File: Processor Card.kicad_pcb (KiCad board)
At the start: 2 copper layers, 100 x 100 mm, 31 parts, among them J1 Conn_02x20_Odd_Even, U1 CDP1802/1806, U10 74LS573, U11 74LS138, U2 28C256, U3 62256, U4 62256, U5 74LS32, U6 74LS20, U7 74LS74, U8 74LS04, U9 74LS74

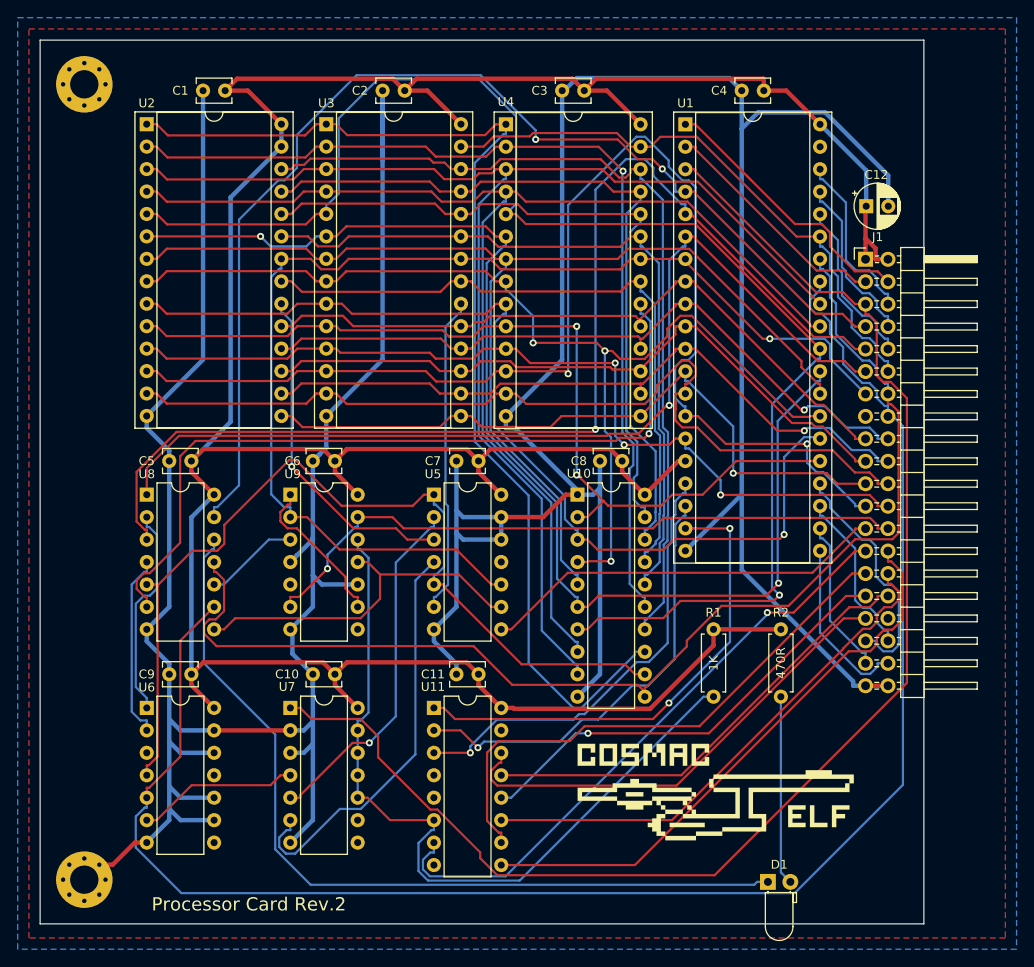
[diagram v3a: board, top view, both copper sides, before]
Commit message: Fix PCB / Schematic mismatch
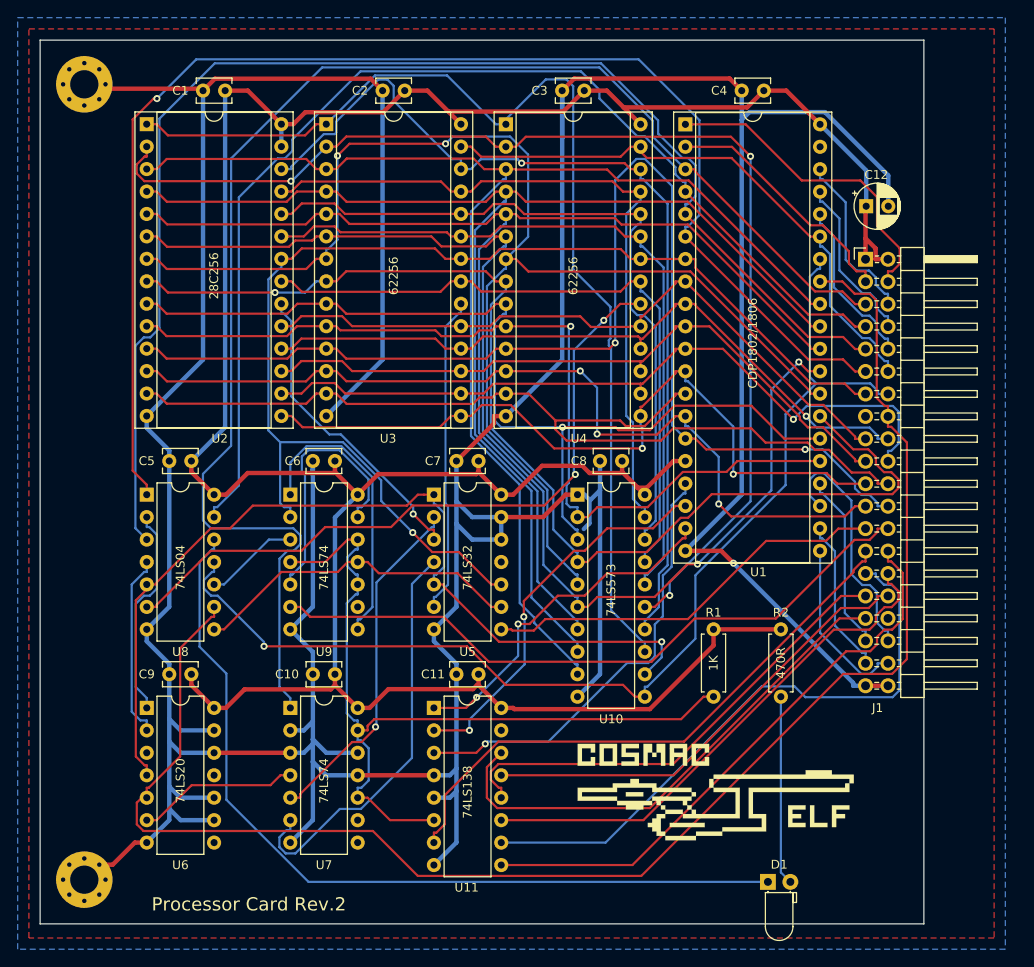
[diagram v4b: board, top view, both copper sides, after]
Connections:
- U7 pad 11: HI -> GND
- U7 pad 12: HI -> GND
- U9 pad 10: GND -> HI
- U9 pad 13: ~{IOR} -> Net-(U9-Pad13)
- U9 pad 4: GND -> HI
- U9 pad 5: unconnected-(U9-Pad5) -> Net-(U9-Pad13)
- U9 pad 8: unconnected-(U9-Pad8) -> Net-(U9-Pad1)
- U9 pad 9: Net-(U9-Pad1) -> unconnected-(U9-Pad9)
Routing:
- net GND: track 544.2 -> 600.8 mm, vias 0 -> 1
- net D1: track 143.1 -> 99.1 mm, vias 2 -> 3
- net SC0: track 111.9 -> 153.6 mm
- net D0: track 100.4 -> 138.2 mm, vias 3 -> 2
- net Net-(U9-Pad13): track 0.00 -> 29.7 mm
- net /A5: track 165.0 -> 137.7 mm, vias 1 -> 0
- net /A12: track 107.9 -> 134.3 mm, vias 1 -> 3
- net /A3: track 128.4 -> 154.0 mm, vias 0 -> 2
- net VCC: track 347.3 -> 322.9 mm
- net SC1: track 131.4 -> 151.5 mm, vias 1 -> 0
- net /N0: track 55.5 -> 39.6 mm
- net Net-(U9-Pad1): track 17.8 -> 33.2 mm
- net /A2: track 119.4 -> 132.4 mm, vias 3 -> 1
- net /Memory Select/~{HI RAM CS}: track 89.6 -> 78.7 mm, vias 1 -> 2
- net TPB: track 188.8 -> 178.5 mm
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
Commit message: Finalised layout
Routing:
- net GND: track 600.8 -> 563.1 mm
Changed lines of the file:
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@@
   (segment (start 192.8211 65.88) (end 194.6972 67.7561) (width 0.25) (layer "F.Cu") (net 1))
   (segment (start 107.8971 55.4971) (end 106.6971 56.6971) (width 0.5) (layer "F.Cu") (net 2))
-  (segment (start 112.065 140.805) (end 110.7149 140.805) (width 0.5) (layer "F.Cu") (net 2))
   (segment (start 107.4 143.3029) (end 106.6971 143.3029) (width 0.5) (layer "F.Cu") (net 2))
   (segment (start 107.4 143.3029) (end 107.4 145) (width 0.5) (layer "F.Cu") (net 2))
@@
   (segment (start 138.7533 55.715) (end 137.4019 54.3636) (width 0.5) (layer "F.Cu") (net 2))
   (segment (start 119.685 130.645) (end 128.3117 130.645) (width 0.5) (layer "F.Cu") (net 2))
-  (segment (start 118.435 55.715) (end 118.2171 55.4971) (width 0.5) (layer "F.Cu") (net 2))
   (segment (start 105.7029 54.2971) (end 105 55) (width 0.5) (layer "F.Cu") (net 2))
   (segment (start 104.0058 57.4) (end 103.3029 56.6971) (width 0.5) (layer "F.Cu") (net 2))
   (segment (start 105 57.4) (end 104.0058 57.4) (width 0.5) (layer "F.Cu") (net 2))
-  (segment (start 110.7149 140.805) (end 108.217 143.3029) (width 0.5) (layer "F.Cu") (net 2))
   (segment (start 195.94 123.057) (end 193.4 123.057) (width 0.5) (layer "F.Cu") (net 2))
   (segment (start 103.3029 143.3029) (end 104.2971 143.3029) (width 0.5) (layer "F.Cu") (net 2))
@@
   (segment (start 106.6971 53.3029) (end 105.7029 53.3029) (width 0.5) (layer "F.Cu") (net 2))
   (segment (start 105.7029 53.3029) (end 105.7029 54.2971) (width 0.5) (layer "F.Cu") (net 2))
-  (segment (start 159.0717 55.715) (end 160.44 54.3467) (width 0.5) (layer "F.Cu") (net 2))
   (segment (start 105.7029 53.3029) (end 105 52.6) (width 0.5) (layer "F.Cu") (net 2))
   (segment (start 177.061 107.79) (end 178.4611 109.1901) (width 0.5) (layer "F.Cu") (net 2))
-  (segment (start 160.44 54.3467) (end 178.0217 54.3467) (width 0.5) (layer "F.Cu") (net 2))
   (segment (start 156.9149 103.975) (end 152.1783 103.975) (width 0.5) (layer "F.Cu") (net 2))
   (segment (start 107.4 55) (end 107.8971 55.4971) (width 0.5) (layer "F.Cu") (net 2))
-  (segment (start 118.2171 55.4971) (end 107.8971 55.4971) (width 0.5) (layer "F.Cu") (net 2))
   (segment (start 104.2971 143.3029) (end 105 142.6) (width 0.5) (layer "F.Cu") (net 2))
   (segment (start 106.6971 146.6971) (end 105.7029 146.6971) (width 0.5) (layer "F.Cu") (net 2))
@@
   (segment (start 105.7029 143.3029) (end 105 142.6) (width 0.5) (layer "F.Cu") (net 2))
   (segment (start 106.6971 143.3029) (end 105.7029 143.3029) (width 0.5) (layer "F.Cu") (net 2))
-  (segment (start 108.217 143.3029) (end 107.4 143.3029) (width 0.5) (layer "F.Cu") (net 2))
   (segment (start 105.7029 146.6971) (end 105 147.4) (width 0.5) (layer "F.Cu") (net 2))
   (segment (start 173.015 107.79) (end 177.061 107.79) (width 0.5) (layer "F.Cu") (net 2))
   (segment (start 137.4019 54.3636) (end 119.7864 54.3636) (width 0.5) (layer "F.Cu") (net 2))
   (segment (start 104.5029 145.4971) (end 105 145) (width 0.5) (layer "F.Cu") (net 2))
-  (segment (start 178.0217 54.3467) (end 179.39 55.715) (width 0.5) (layer "F.Cu") (net 2))
   (segment (start 103.3029 146.6971) (end 104.2971 146.6971) (width 0.5) (layer "F.Cu") (net 2))
   (segment (start 104.2971 146.6971) (end 104.2971 145.7029) (width 0.5) (layer "F.Cu") (net 2))
